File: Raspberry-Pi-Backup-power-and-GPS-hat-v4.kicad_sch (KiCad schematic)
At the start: 12 parts, among them J1 GPIO, U1 ESP32-DEVKIT-V1, U2 MAX-F10S-00B

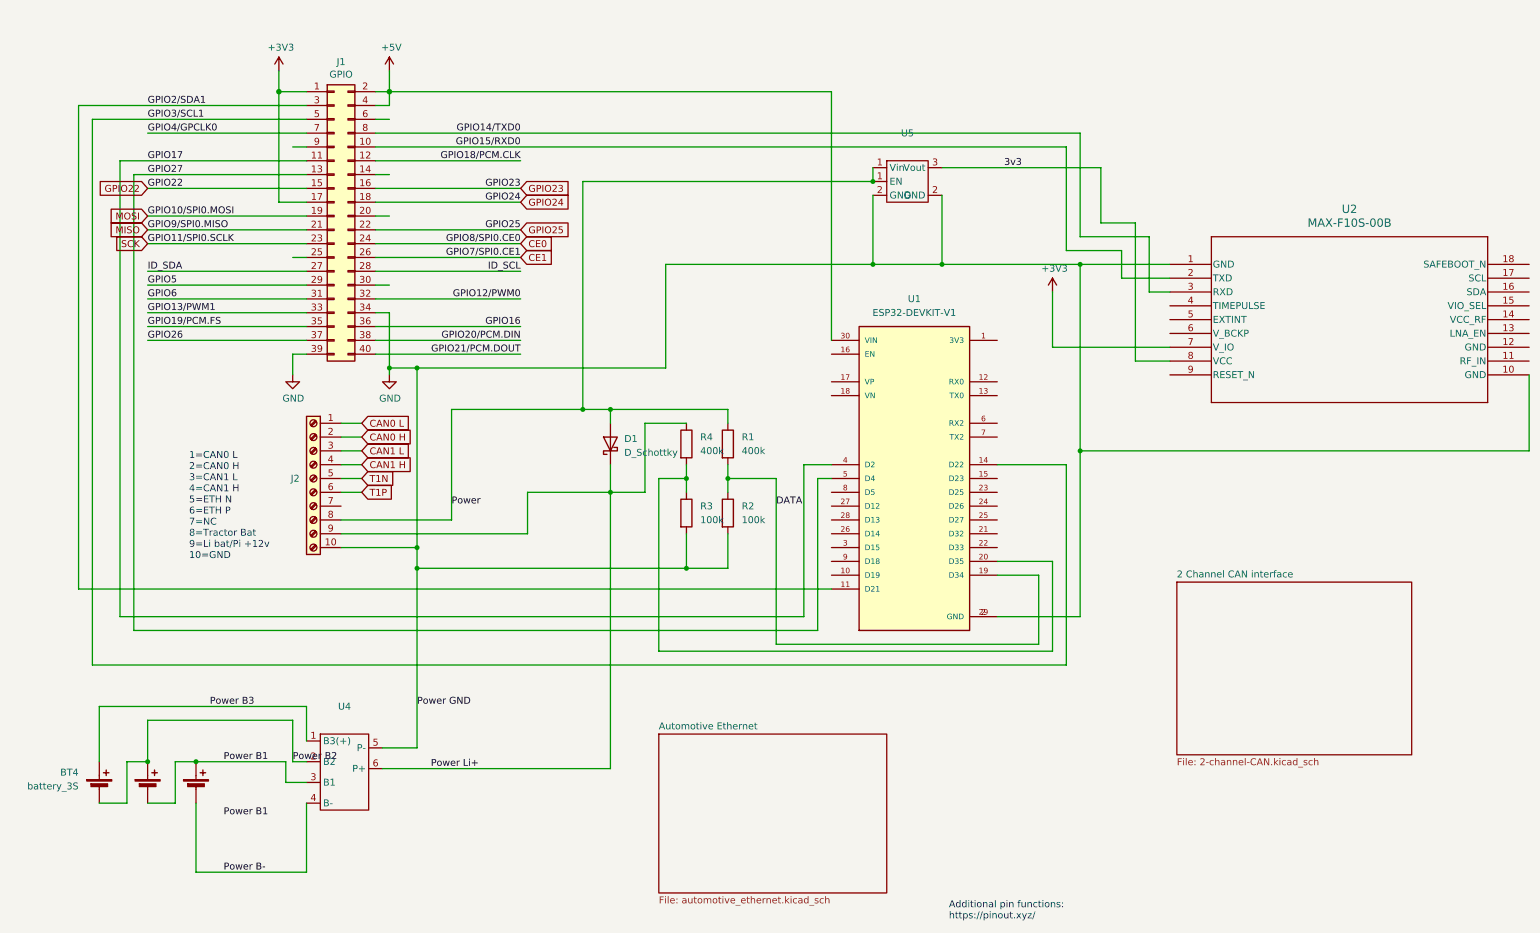
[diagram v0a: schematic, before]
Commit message: Remove non-existent security fields from bluer characteristics
The bluer crate's CharacteristicWrite and CharacteristicNotify
don't have encrypt_*/secure_* fields - removed them.

Co-Authored-By: Claude Opus 4.5 <noreply@anthropic.com>
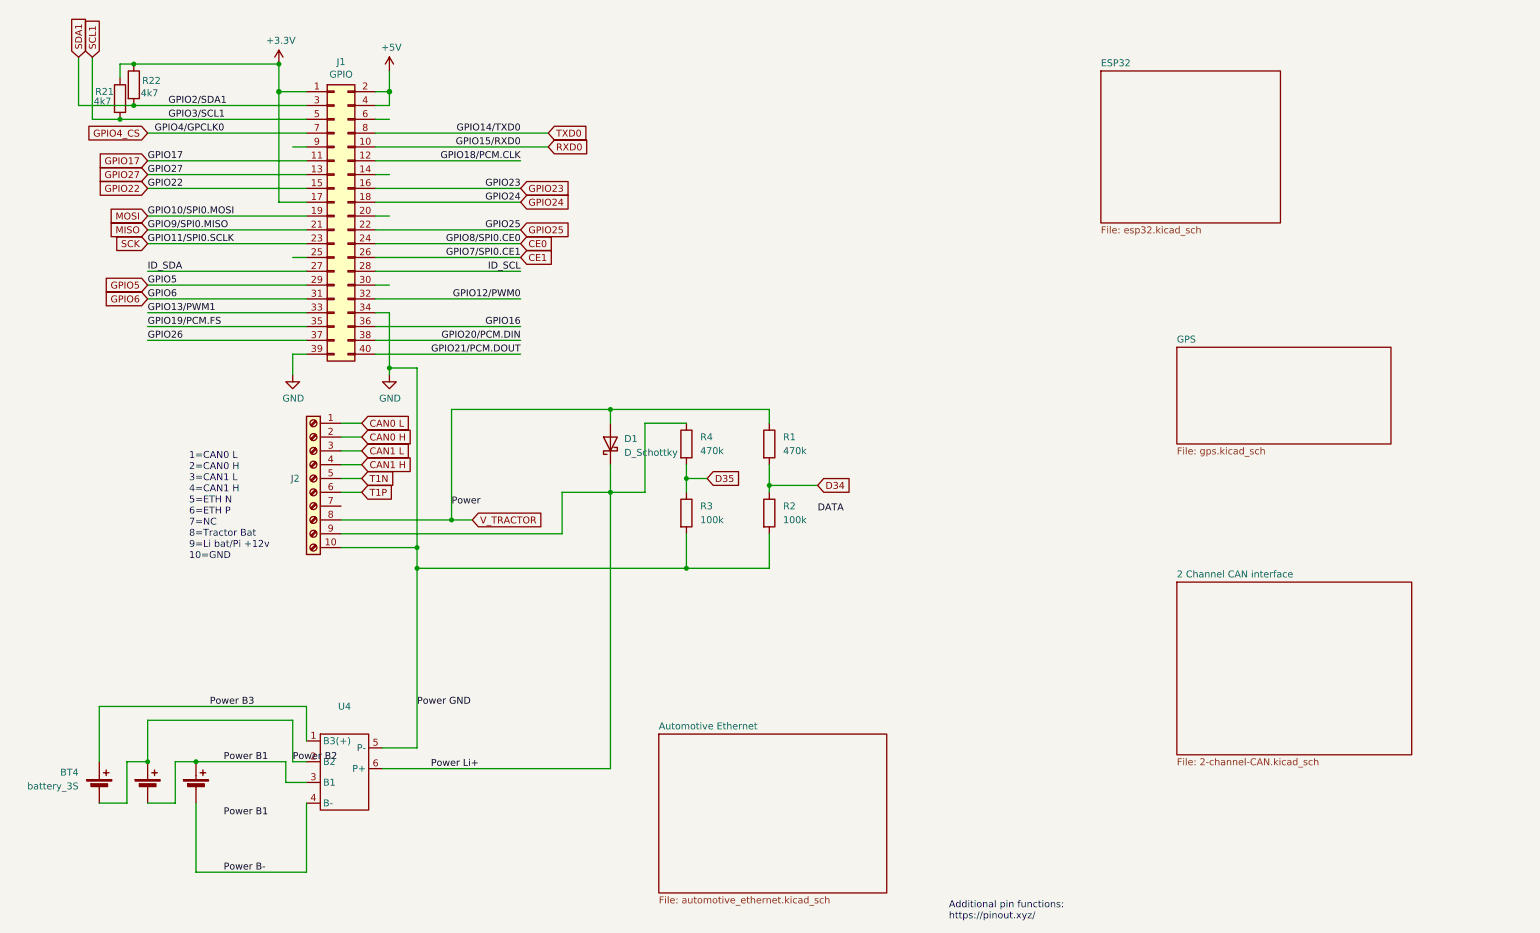
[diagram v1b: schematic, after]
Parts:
- removed U1: ESP32-DEVKIT-V1, ESP32-DEVKIT-V1:MODULE_ESP32_DEVKIT_V1, symbol ESP32-DEVKIT-V1:ESP32-DEVKIT-V1
- removed U2: MAX-F10S-00B, MAX-F10S_UBL, symbol Ublox F10S Max:MAX-F10S-00B
- removed U5: ~, Perfect Precision:MP4560, symbol Perfect Precision:MP4560
- added R21, R22: 4k7, Resistor_SMD:R_0402_1005Metric, symbol Device:R
- BT4, J1, U4: now left out of the parts list
- D1: footprint Diode_THT:D_A-405_P7.62mm_Horizontal -> Diode_SMD:D_SMC
- J2: footprint TerminalBlock_CUI:TerminalBlock_CUI_TB007-508-08_1x08_P5.08mm_Horizontal -> TerminalBlock_CUI:TerminalBlock_CUI_TB007-508-10_1x10_P5.08mm_Horizontal; now left out of the parts list
- R1, R4: value 400k -> 470k
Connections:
- net DATA: no longer R1.2, R2.1
- net D35: now reaches R3.1, R4.2
- net +3V3 renamed +3.3V
- net +3.3V: now also R21.1, R22.1
- net GPIO14/TXD0 renamed TXD0
- net GPIO15/RXD0 renamed RXD0
- net GPIO2/SDA1 renamed SDA1
- net SDA1: now also R22.2
- net GPIO3/SCL1 renamed SCL1
- net SCL1: now also R21.2
- net GPIO4/GPCLK0 renamed GPIO4_CS
- net Power renamed V_TRACTOR
- new net D34: R1.2, R2.1
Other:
- added sheet ESP32 (esp32.kicad_sch)
- added sheet GPS (gps.kicad_sch)
- moved on the sheet: R1, R2
